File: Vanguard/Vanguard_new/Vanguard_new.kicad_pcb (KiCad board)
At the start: 2 copper layers, 45.5 x 50 mm, 52 parts, among them J1 USB_C, J2 Conn_02x03_Pin, J3 Micro_SD_Card_Det1, Q1 BSS138, Q2 BSS138, Q3 BSS138, U1 ATSAMD11D14A-M, U2 ATmega4809-A, U3 AT25DF641A-SH-T, U4 AP2112K-3.3, U5 MPM3610AGQV-P, U7 TXB0104D, Y1 32.768kHz

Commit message: starting work on pcb, imported parts
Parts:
- added U6: BNO086, BNO086:IC_BNO086, F.Cu at (27.2, 48.9)

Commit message: finished footprints + moved to pcb
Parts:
- moved ADR1 190.4 mm to (142.1, 97.7)
- moved D1 190.4 mm to (163.4, 77.7)
- moved D2 190.4 mm to (162.7, 80.8)
- moved D3 190.4 mm to (162.7, 82.5)
- moved D5 190.4 mm to (162.7, 84.3)
- moved D6 190.4 mm to (137.1, 97.6)
- moved Q1 190.4 mm to (148.1, 88.1)
- moved Q2 190.4 mm to (148.1, 92.7)
- moved Q3 190.4 mm to (148.1, 97.3)
- moved R15 190.4 mm to (156.3, 59.0)
- moved R16 190.4 mm to (156.3, 61.0)
- moved R17 190.4 mm to (156.3, 63.0)
- moved R18 190.4 mm to (156.3, 64.9)
- moved R19 190.4 mm to (156.3, 66.9)
- moved R20 190.4 mm to (156.3, 68.9)
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
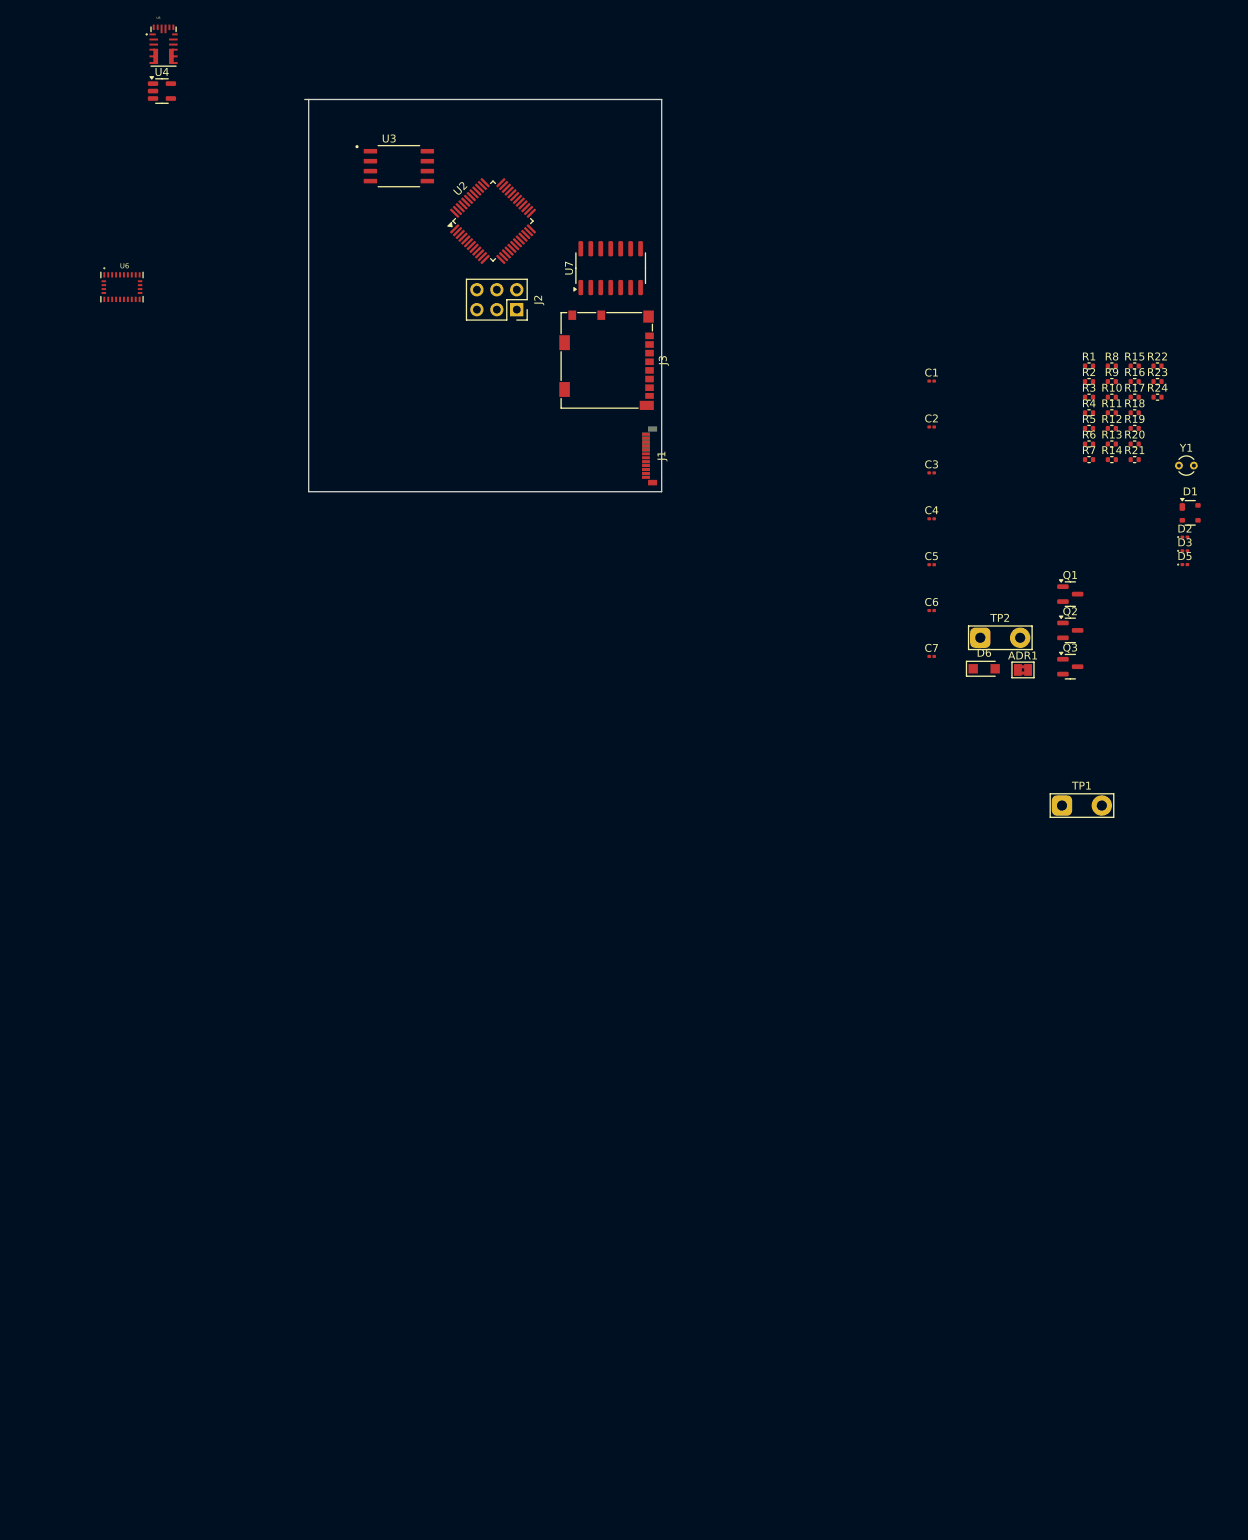
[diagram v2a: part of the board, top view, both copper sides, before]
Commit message: moved and wired 1 part
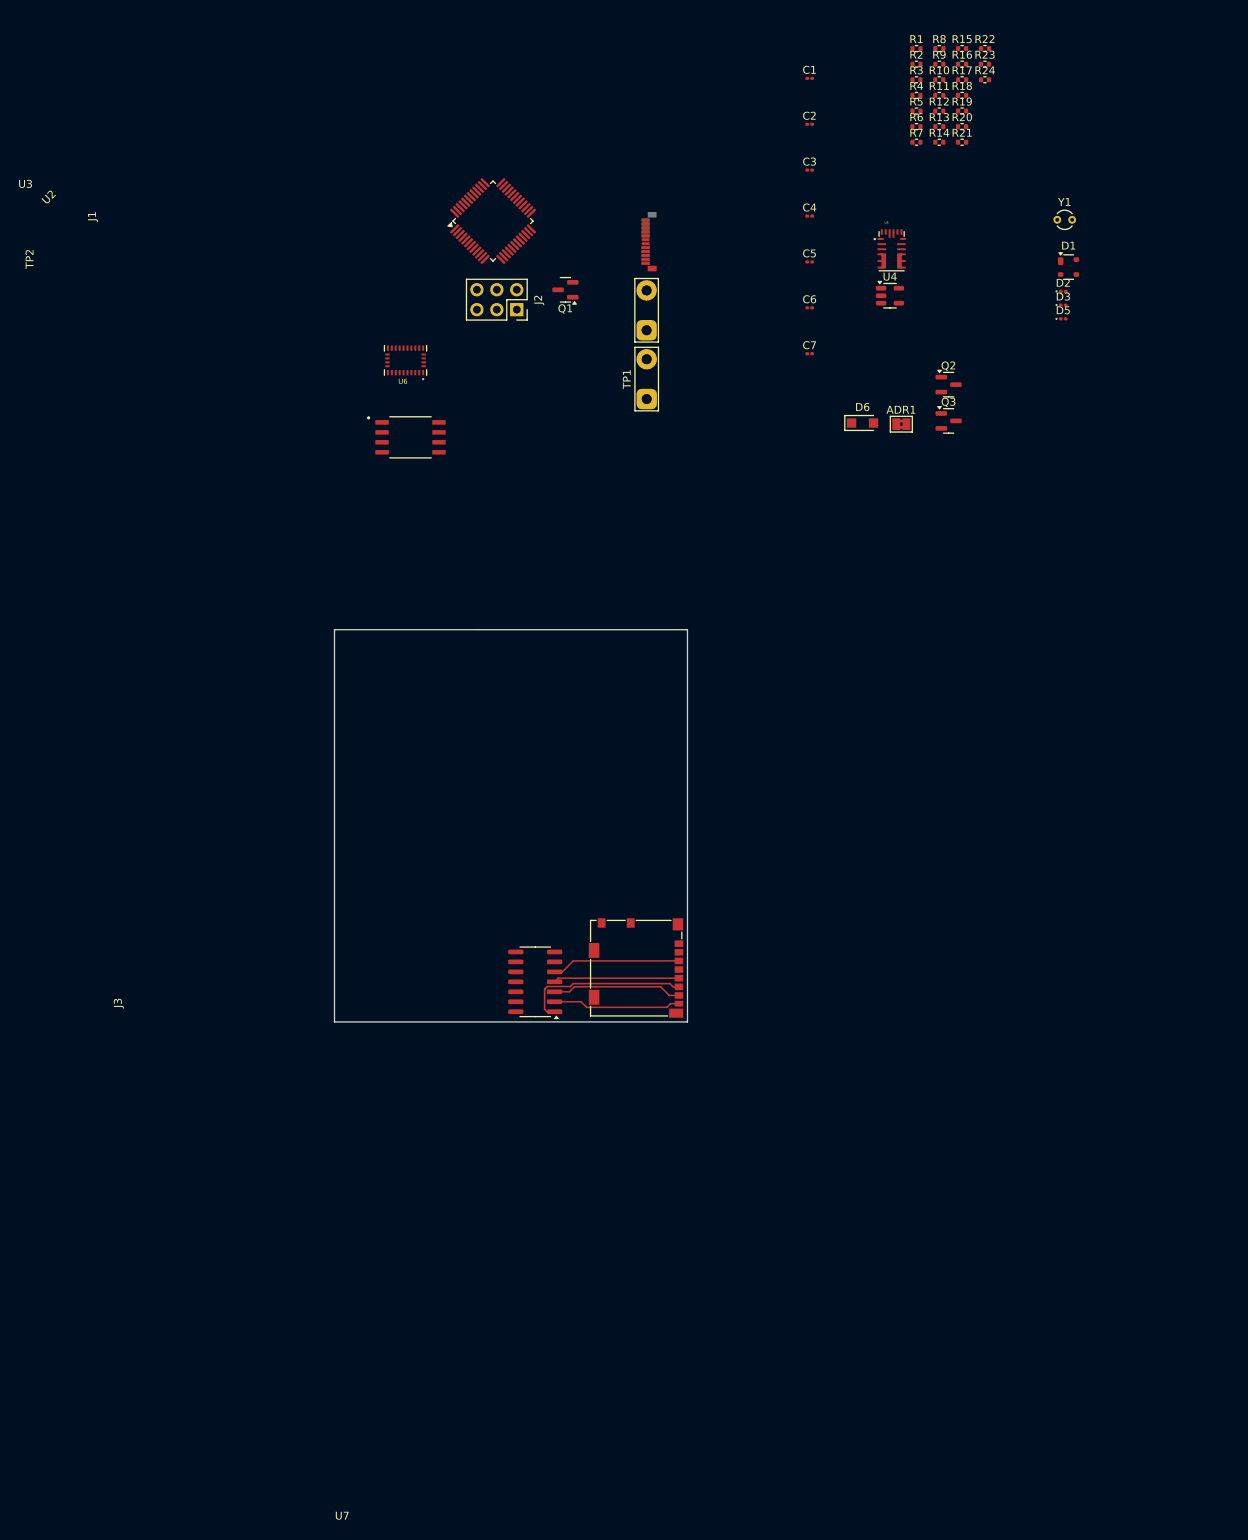
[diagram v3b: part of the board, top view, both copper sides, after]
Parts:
- moved U4 96.4 mm to (125.1, 50.0)
- moved U5 96.4 mm to (125.3, 44.3)
- moved U7 91.5 mm to (79.9, 137.5), turned to 180 degrees
- moved J3 77.6 mm to (92.8, 135.7)
- moved Q1 75.1 mm to (83.7, 49.3), turned to 180 degrees
- moved TP1 74.1 mm to (94.1, 63.2), turned to 90 degrees
- moved TP2 57.8 mm to (94.1, 54.4), turned to 90 degrees
- moved R10 46.1 mm to (131.4, 22.5)
- moved R12 46.1 mm to (131.4, 26.5)
- moved R13 46.1 mm to (131.4, 28.5)
- moved R16 46.1 mm to (134.3, 20.5)
- moved R17 46.1 mm to (134.3, 22.5)
- moved R19 46.1 mm to (134.3, 26.5)
- moved R2 46.1 mm to (128.5, 20.5)
- moved R20 46.1 mm to (134.3, 28.5)
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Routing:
- net RST: track 0.00 -> 21.6 mm
- net Net-(J3-DAT0): track 0.00 -> 16.6 mm
- net Net-(J3-CMD): track 0.00 -> 16.4 mm
- net Net-(J3-DAT1): track 0.00 -> 16.3 mm
- net Net-(J3-CLK): track 0.00 -> 16.0 mm
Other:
- board size 45.5 x 50 mm -> 45 x 50 mm
- copper layers 2 -> 4

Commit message: symbol adressing, and pcb layout
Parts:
- added PORTSIDE_RGB1: SMLVN6RGB, LED_SMD:LED_ROHM_SMLVN6, F.Cu at (64.5, 104.5)
- added Q4: BSS138, Package_TO_SOT_SMD:SOT-23, F.Cu at (84.5, 120.5)
- added STARBOARD_RGB1: SMLVN6RGB, LED_SMD:LED_ROHM_SMLVN6, F.Cu at (90.0, 104.0)
- added U8: TPS61092, Package_DFN_QFN:Texas_RSA_VQFN-16-1EP_4x4mm_P0.65mm_EP2.7x2.7mm_ThermalVias, F.Cu at (73.4, 127.1)
- moved U1 160.7 mm to (81.1, 127.1)
- moved U5 110.1 mm to (69.0, 139.0)
- moved J1 100.8 mm to (60.5, 138.2)
- moved U4 97.3 mm to (62.5, 124.5)
- moved Q2 94.9 mm to (66.5, 129.5), turned to 180 degrees
- moved Q3 93.6 mm to (62.6, 128.1), turned to 180 degrees
- moved D6 92.5 mm to (64.5, 139.0), turned to 90 degrees
- moved Q1 78.6 mm to (66.5, 125.9)
- moved U2 73.8 mm to (77.3, 114.2)
- moved J2 69.1 mm to (91.5, 119.4), turned to 0 degrees
- moved ADR1 60.7 mm to (82.3, 108.0)
- moved U3 51.1 mm to (68.5, 119.0), turned to -45 degrees
- moved U6 48.7 mm to (77.2, 104.9), turned to 0 degrees
- moved D5 12.1 mm to (141.3, 63.5)
- moved U7 2.88 mm to (77.0, 137.5), turned to 0 degrees
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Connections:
- U2 pad 10: unconnected-(U2-PC0-Pad10) -> STAR_RED
- U2 pad 11: unconnected-(U2-PC1-Pad11) -> STAR_GREEN
- U2 pad 12: unconnected-(U2-PC2-Pad12) -> STAR_BLUE
- U2 pad 13: unconnected-(U2-PC3-Pad13) -> PORT_SERVO
- U2 pad 16: unconnected-(U2-PC4-Pad16) -> BUZZER
- U2 pad 30: unconnected-(U2-PE0-Pad30) -> PORT_RED
- U2 pad 34: unconnected-(U2-PF0-Pad34) -> PORT_GREEN
- U2 pad 35: unconnected-(U2-PF1-Pad35) -> PORT_BLUE
- U2 pad 36: unconnected-(U2-PF2-Pad36) -> STAR_SERVO
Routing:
- net Net-(J3-DAT0): track 16.6 -> 0.00 mm
- net Net-(J3-CMD): track 16.4 -> 0.00 mm
- net Net-(J3-DAT1): track 16.3 -> 0.00 mm
- net Net-(J3-CLK): track 16.0 -> 0.00 mm
- net RST: track 21.6 -> 20.6 mm
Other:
- board size 45 x 50 mm -> 45 x 50.1 mm

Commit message: ref prev.
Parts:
- added BZ1: Buzzer, Buzzer_Beeper:Buzzer_TDK_PS1240P02BT_D12.2mm_H6.5mm, F.Cu at (73.6, 100.0)
- added C10: 100 uF, Capacitor_SMD:C_0201_0603Metric, F.Cu at (79.2, 44.0)
- added C8: 10 uF, Capacitor_SMD:C_0201_0603Metric, F.Cu at (79.2, 40.5)
- added C9: 2.2uF, Capacitor_SMD:C_0201_0603Metric, F.Cu at (79.2, 42.2)
- added J4: STARBOARD_SERVO, Connector_PinHeader_2.54mm:PinHeader_1x03_P2.54mm_Vertical, F.Cu at (88.0, 109.0)
- added J5: PORTSIDE_SERVO, Connector_PinHeader_2.54mm:PinHeader_1x03_P2.54mm_Vertical, F.Cu at (62.5, 109.0)
- added L1: 6.8 uH, Inductor_SMD:L_0402_1005Metric, F.Cu at (67.2, 26.9)
- added R25: 220, Resistor_SMD:R_0402_1005Metric, F.Cu at (67.2, 28.9)
- added R26: 220, Resistor_SMD:R_0402_1005Metric, F.Cu at (67.2, 30.9)
- added R27: 220, Resistor_SMD:R_0402_1005Metric, F.Cu at (67.2, 32.8)
- added R28: 220, Resistor_SMD:R_0402_1005Metric, F.Cu at (67.2, 34.8)
- added R29: 220, Resistor_SMD:R_0402_1005Metric, F.Cu at (67.2, 36.8)
- added R30: 220, Resistor_SMD:R_0402_1005Metric, F.Cu at (67.2, 38.8)
- J2: footprint Connector_PinSocket_2.54mm:PinSocket_2x03_P2.54mm_Vertical -> Connector_PinHeader_2.54mm:PinHeader_1x03_P2.54mm_Vertical
- moved U6 9.45 mm to (68.8, 109.1)

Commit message: pcb work
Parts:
- moved L1 196.0 mm to (241.5, 116.7)
- moved C10 196.0 mm to (253.4, 133.8)
- moved C8 196.0 mm to (253.4, 130.3)
- moved C9 196.0 mm to (253.4, 132.0)
- moved U8 195.6 mm to (269.0, 125.7)
- moved BZ1 195.2 mm to (268.1, 82.8), turned to 180 degrees
- moved Q4 178.7 mm to (260.7, 90.4), turned to 180 degrees
- moved U4 174.6 mm to (210.2, 31.6)
- moved U5 172.9 mm to (204.4, 31.4)
- moved R25 159.4 mm to (212.4, 94.6), turned to 180 degrees
- moved R26 158.1 mm to (212.4, 93.5), turned to 180 degrees
- moved R27 156.9 mm to (212.4, 92.3), turned to 180 degrees
- moved D6 147.6 mm to (183.8, 52.2)
- moved R28 144.8 mm to (200.1, 92.3), turned to 180 degrees
- moved R29 144.4 mm to (200.1, 93.3), turned to 180 degrees
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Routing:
- net Net-(J3-DAT1): track 0.00 -> 15.4 mm
- net Net-(J3-DAT0): track 0.00 -> 15.4 mm
- net Net-(J3-CMD): track 0.00 -> 15.3 mm
- net RST: track 20.6 -> 35.7 mm
- net Net-(J3-CLK): track 0.00 -> 14.9 mm
- net GND: track 0.00 -> 12.0 mm, vias 0 -> 6
- net Net-(BZ1--): track 0.00 -> 7.23 mm
- net Net-(U6-XIN32): track 0.00 -> 5.32 mm
- net Net-(U6-XOUT32/CLKSEL1): track 0.00 -> 5.21 mm
- net Net-(ADR1-B): track 0.00 -> 4.43 mm
- net Net-(U5-VIN): track 0.00 -> 3.42 mm
- net Net-(STARBOARD_RGB1-BA): track 0.00 -> 1.57 mm
- net Net-(STARBOARD_RGB1-RA): track 0.00 -> 1.54 mm
- net Net-(PORTSIDE_RGB1-GA): track 0.00 -> 1.53 mm
- net Net-(STARBOARD_RGB1-GA): track 0.00 -> 1.53 mm
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- added copper zone on B.Cu, net (none)
- added copper zone on F.Cu, net (none)
- added copper zone on In1.Cu, net GND
- added copper zone on In2.Cu, net GND
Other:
- board size 45 x 50.1 mm -> 628.1 x 251 mm
